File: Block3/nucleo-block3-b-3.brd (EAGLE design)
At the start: 100.3 x 80 mm, 91 parts, among them IC1 TL331, J4 MODJACK6P6C-MJ3245-66-0CONN_M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, J5 MODJACK6P6C-MJ3245-66-0CONN_M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, Q1 NPN-23, Q2 BSS123, Q3 BSS84, U1 TC4428, U2 TC4428, U3 TC4428

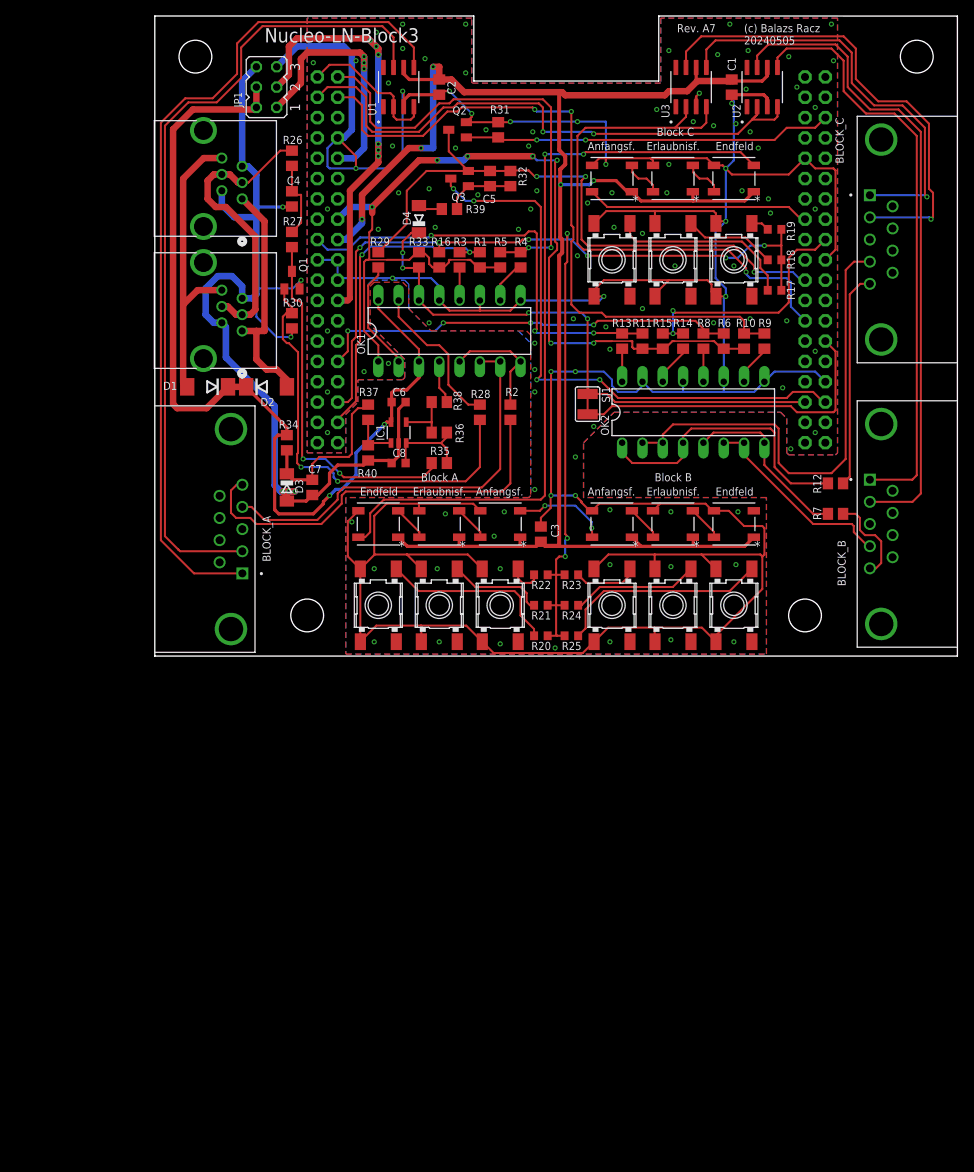
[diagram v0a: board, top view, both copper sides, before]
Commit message: - adds a small TH pin "alignment hole" to the lib - fixes the DB-9 connector's pin order - updates the loconet-block3 board for rev B.
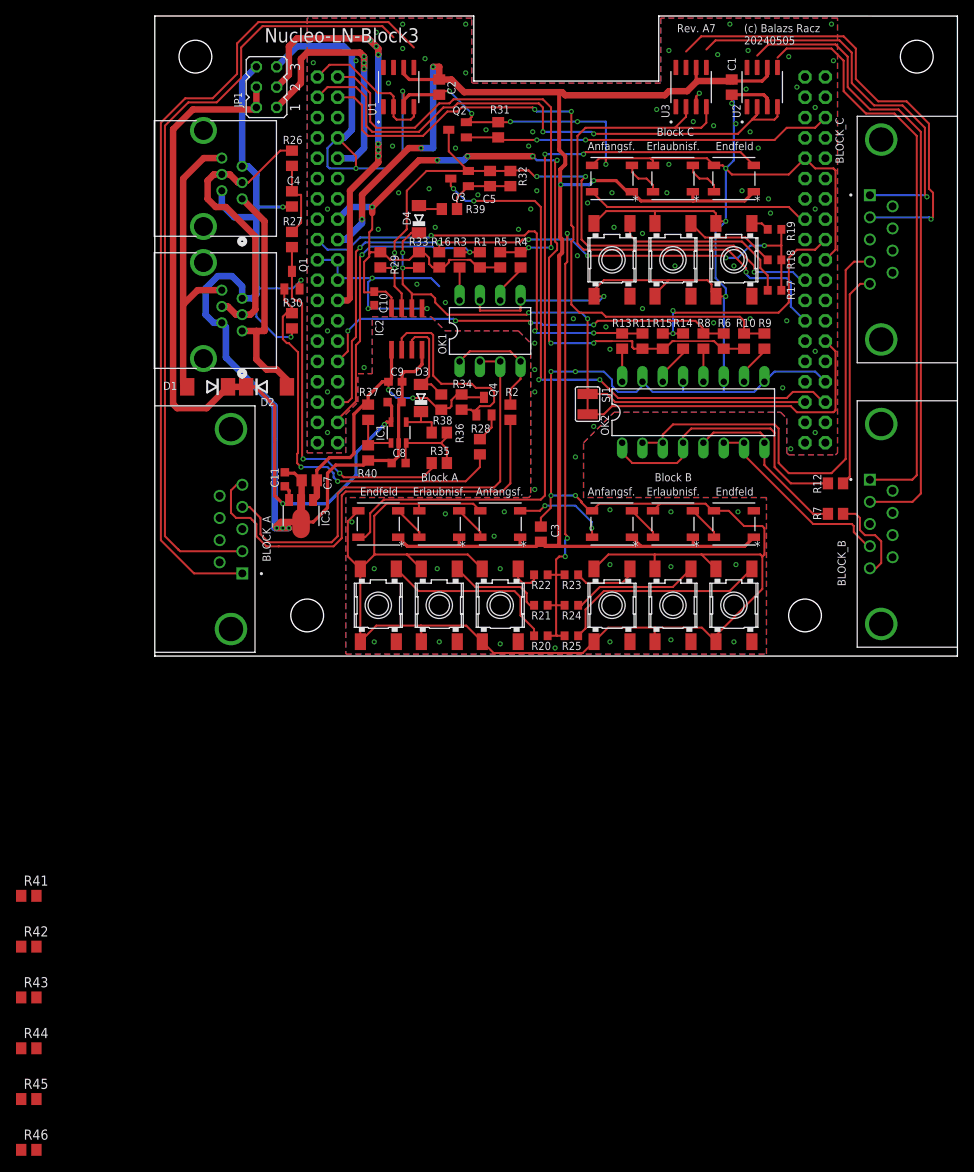
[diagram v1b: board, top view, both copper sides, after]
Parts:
- added C10, C9: (no value), rcl:C0603
- added C11: (no value), rcl:C0603K
- added IC2: ISO7221A, texas:SO-08
- added IC3: 78L05F, linear:SOT89
- added Q4: BSS84, eagleparts:SOT23-PCH
- added R41, R42, R43, R44, R45, R46: 100, rcl:R0805
- D3: value 5V1 -> (none); device diode:SOD80C -> diode:MINIMELF
- OK1: value PC847 -> PC827; device optocoupler:DIL16 -> optocoupler:DIL08
- R29: value 200 -> 10k
- R34: value 1k -> 10k
- R38: value 1k5 -> 10k
- moved R34 22.4 mm to (38.4, 31.8), turned to 90 degrees
- moved D3 20.1 mm to (33.3, 32.3), turned to 90 degrees
- moved OK1 5.08 mm to (41.9, 40.6)
- moved R28 4.32 mm to (40.6, 26.2)
- moved C7 0.97 mm to (19.3, 22.0), turned to 0 degrees
- moved C6 0.51 mm to (30.0, 31.8)
- moved R29 0.25 mm to (28.2, 49.5), turned to 270 degrees
- moved R38 0.25 mm to (35.8, 31.8), turned to 270 degrees
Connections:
- new net N$20: D3.A, IC2.3, R38.1
- new net N$24: R41.1, U1.7
- new net N$25: R42.1, U1.5
- new net N$37: R43.1, U2.7
- new net N$40: R46.1, U3.5
- new net N$8: IC2.2, Q4.1, R34.1
- net AGND: now also C11.1, C9.1, IC2.4, IC3.2, IC3.2@1; no longer D3.A
- net BLKA-RX-: now also OK1.2, OK1.3; no longer OK1.6, OK1.7
- net BLKA-TX+: now also R42.2; no longer U1.5
- net BLKA-TX-: now also R41.2; no longer U1.7
- net BLKB-TX+: now also R44.2; no longer U2.5
- net BLKB-TX-: now also R43.2; no longer U2.7
- net BLKC-TX+: now also R46.2; no longer U3.5
- net BLKC-TX-: now also R45.2; no longer U3.7
- net GND: now also C10.2, IC2.5, OK1.5, OK1.7; no longer OK1.11, OK1.13, OK1.9
- net LN-RX: now also IC2.6; no longer OK1.14
- net LN-TX: now also IC2.7
- net LN5V: now also C9.2, IC2.1, IC3.1, Q4.3, R38.2; no longer D3.C
- net LNPLUS: now also C11.2, IC3.3; no longer OK1.16, OK1.3, R34.1
- net N$11: now also Q4.2; no longer OK1.15
- net N$31: now also OK1.1, OK1.4; no longer OK1.5, OK1.8
- net N$36: now also D3.C; no longer R38.1
- net N$38: now also R44.1, U2.5; no longer OK1.2, R29.1
- net N$39: now also R45.1, U3.7; no longer OK1.4, R38.2
- net N$41: now also OK1.8; no longer OK1.12
- net N$42: now also OK1.6; no longer OK1.10
- net VCC: now also C10.1, IC2.8, R29.1; no longer OK1.1
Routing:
- net N$8: track 0.00 -> 26.0 mm
- net AGND: track 126.3 -> 150.0 mm
- net LN5V: track 21.3 -> 40.6 mm, vias 0 -> 2
- net LNPLUS: track 118.6 -> 101.1 mm
- net N$11: track 19.0 -> 3.63 mm
- net N$38: track 13.9 -> 0.00 mm
- net N$20: track 0.00 -> 12.8 mm
- net LN-TX: track 77.6 -> 85.9 mm, vias 3 -> 5
- net BLKA-RX-: track 52.0 -> 59.1 mm
- net GND: track 508.9 -> 515.3 mm, vias 113 -> 115
- net BLKA-RX+: track 50.7 -> 56.4 mm
- net N$39: track 5.47 -> 0.00 mm
- net LN-TX-B: track 54.8 -> 50.4 mm
- net VCC: track 120.1 -> 116.0 mm
- net BLKA-TX-: track 102.1 -> 98.3 mm
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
